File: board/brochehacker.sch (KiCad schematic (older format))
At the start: 5 parts, among them IC1 ATTINY85-P, P1 CONN_01X02, U1 MAX7219

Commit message: adição de chave de força
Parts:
- added SW1: SPST, Buttons_Switches_ThroughHole:SW_DIP_x1_Slide, symbol SPST
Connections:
- wire segments 53 -> 52
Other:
- moved on the sheet: P1
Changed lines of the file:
@@
 L CONN_01X02 P1
 U 1 1 579A841D
-P 7650 4800
-F 0 "P1" H 7650 4950 50  0000 C CNN
-F 1 "CONN_01X02" V 7750 4800 50  0000 C CNN
-F 2 "Pin_Headers:Pin_Header_Straight_1x02" H 7650 4800 50  0001 C CNN
-F 3 "" H 7650 4800 50  0000 C CNN
-	1    7650 4800
+P 8200 4750
+F 0 "P1" H 8200 4900 50  0000 C CNN
+F 1 "CONN_01X02" V 8300 4750 50  0000 C CNN
+F 2 "Pin_Headers:Pin_Header_Straight_1x02" H 8200 4750 50  0001 C CNN
+F 3 "" H 8200 4750 50  0000 C CNN
+	1    8200 4750
 	1    0    0    -1
 $EndComp
-Text GLabel 7250 4750 0    60   Input ~ 0
+Text GLabel 6700 4700 0    60   Input ~ 0
 VCC
-Text GLabel 7250 4850 0    60   Input ~ 0
+Text GLabel 7800 4800 0    60   Input ~ 0
 GND
 Wire Wire Line
-	7250 4750 7450 4750
+	7800 4700 8000 4700
 Wire Wire Line
-	7250 4850 7450 4850
+	7800 4800 8000 4800
+$Comp
+L SPST SW1
+U 1 1 579FD200
+P 7300 4700
+F 0 "SW1" H 7300 4800 50  0000 C CNN
+F 1 "SPST" H 7300 4600 50  0000 C CNN
+F 2 "Buttons_Switches_ThroughHole:SW_DIP_x1_Slide" H 7300 4700 50  0001 C CNN
+F 3 "" H 7300 4700 50  0000 C CNN
+	1    7300 4700
+	-1   0    0    -1
+$EndComp
 Wire Wire Line
-	7350 4850 7350 4950
-Connection ~ 7350 4850
-Wire Wire Line
-	7350 4750 7350 4650
-Connection ~ 7350 4750
-$Comp
-L VCC #PWR01
-U 1 1 579A854E
-P 7350 4650
-F 0 "#PWR01" H 7350 4500 50  0001 C CNN
-F 1 "VCC" H 7350 4800 50  0000 C CNN
-F 2 "" H 7350 4650 50  0000 C CNN
-F 3 "" H 7350 4650 50  0000 C CNN
-	1    7350 4650
-	1    0    0    -1
-$EndComp
-$Comp
-L GND #PWR02
-U 1 1 579A856C
-P 7350 4950
-F 0 "#PWR02" H 7350 4700 50  0001 C CNN
-F 1 "GND" H 7350 4800 50  0000 C CNN
-F 2 "" H 7350 4950 50  0000 C CNN
-F 3 "" H 7350 4950 50  0000 C CNN
-	1    7350 4950
-	1    0    0    -1
-$EndComp
+	6700 4700 6800 4700
 $EndSCHEMATC

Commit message: versão camada simples
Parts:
- removed IC1: ATTINY85-P, Housings_DIP:DIP-8_W7.62mm, symbol ATTINY85-P
- removed SW1: SPST, Buttons_Switches_ThroughHole:SW_DIP_x1_Slide, symbol SPST
- removed U1: MAX7219, Housings_DIP:DIP-24_W7.62mm, symbol MAX7219
- added C1, C3: 22pF, Capacitors_ThroughHole:C_Disc_D3_P2.5, symbol C
- added C2: 100uF, Capacitors_ThroughHole:C_Radial_D5_L6_P2.5, symbol CP
- added IC1: ATMEGA328-P, Housings_DIP:DIP-28_W7.62mm_LongPads, symbol ATMEGA328-P
- added Y1: 16MHz, Crystals:Crystal_HC50-U_Vertical, symbol Crystal
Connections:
- net GND: now also C2.2, IC1.22 (GND), IC1.8 (GND)
- net VCC: now also P1.1 (P1), C1.2, C2.1, C3.2, IC1.20 (AVCC), IC1.7 (VCC)
- net at R1.2: now also IC1.1 ((PCINT14/~RESET~)PC6)
- net DIG0 renamed ROW1
- net ROW1: now also IC1.15 ((PCINT1/OC1A)PB1)
- net DIG1 renamed ROW2
- net ROW2: now also IC1.26 ((PCINT11/ADC3)PC3)
- net DIG2 renamed ROW3
- net ROW3: now also IC1.14 ((PCINT0/CLKO/ICP1)PB0)
- net DIG3 renamed ROW4
- net ROW4: now also IC1.24 ((PCINT9/ADC1)PC1)
- net DIG4 renamed ROW5
- net ROW5: now also IC1.2 ((PCINT16/RXD)PD0)
- net DIG5 renamed ROW6
- net ROW6: now also IC1.13 ((PCINT23/AIN1)PD7)
- net DIG6 renamed ROW7
- net ROW7: now also IC1.3 ((PCINT17/TXD)PD1)
- net DIG7 renamed ROW8
- net ROW8: now also IC1.11 ((PCINT21/OC0B/T1)PD5)
- net SEGA renamed COL2
- net COL2: now also IC1.4 ((PCINT18/INT0)PD2)
- net SEGB renamed COL3
- net COL3: now also IC1.5 ((PCINT19/OC2B/INT1)PD3)
- net SEGC renamed COL4
- net COL4: now also IC1.16 ((PCINT2/OC1B/~SS~)PB2)
- net SEGD renamed COL5
- net COL5: now also IC1.12 ((PCINT22/OC0A/AIN0)PD6)
- net SEGDP renamed COL1
- net COL1: now also IC1.25 ((PCINT10/ADC2)PC2)
- net SEGE renamed COL6
- net COL6: now also IC1.23 ((PCINT8/ADC0)PC0)
- net SEGF renamed COL7
- net COL7: now also IC1.27 ((PCINT12/SDA/ADC4)PC4)
- net SEGG renamed COL8
- net COL8: now also IC1.28 ((PCINT13/SCL/ADC5)PC5)
- new net: C1.1, IC1.10 ((PCINT7/XTAL2/TOSC2)PB7), Y1.1
- new net: C3.1, IC1.9 ((PCINT6/XTAL1/TOSC1)PB6), Y1.2

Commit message: conserta cristal e reajusta jumpers
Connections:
- net GND: now also C1.2, C3.2
- net VCC: no longer C1.2, C3.2
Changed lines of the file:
@@
 	1    0    0    -1
 $EndComp
-Text GLabel 7600 2600 2    60   Input ~ 0
-VCC
 Text GLabel 3550 2000 0    60   Input ~ 0
 VCC
@@
 	3700 3050 3700 2000
 Connection ~ 3700 2000
+Text GLabel 7600 2600 2    60   Input ~ 0
+GND
 $EndSCHEMATC

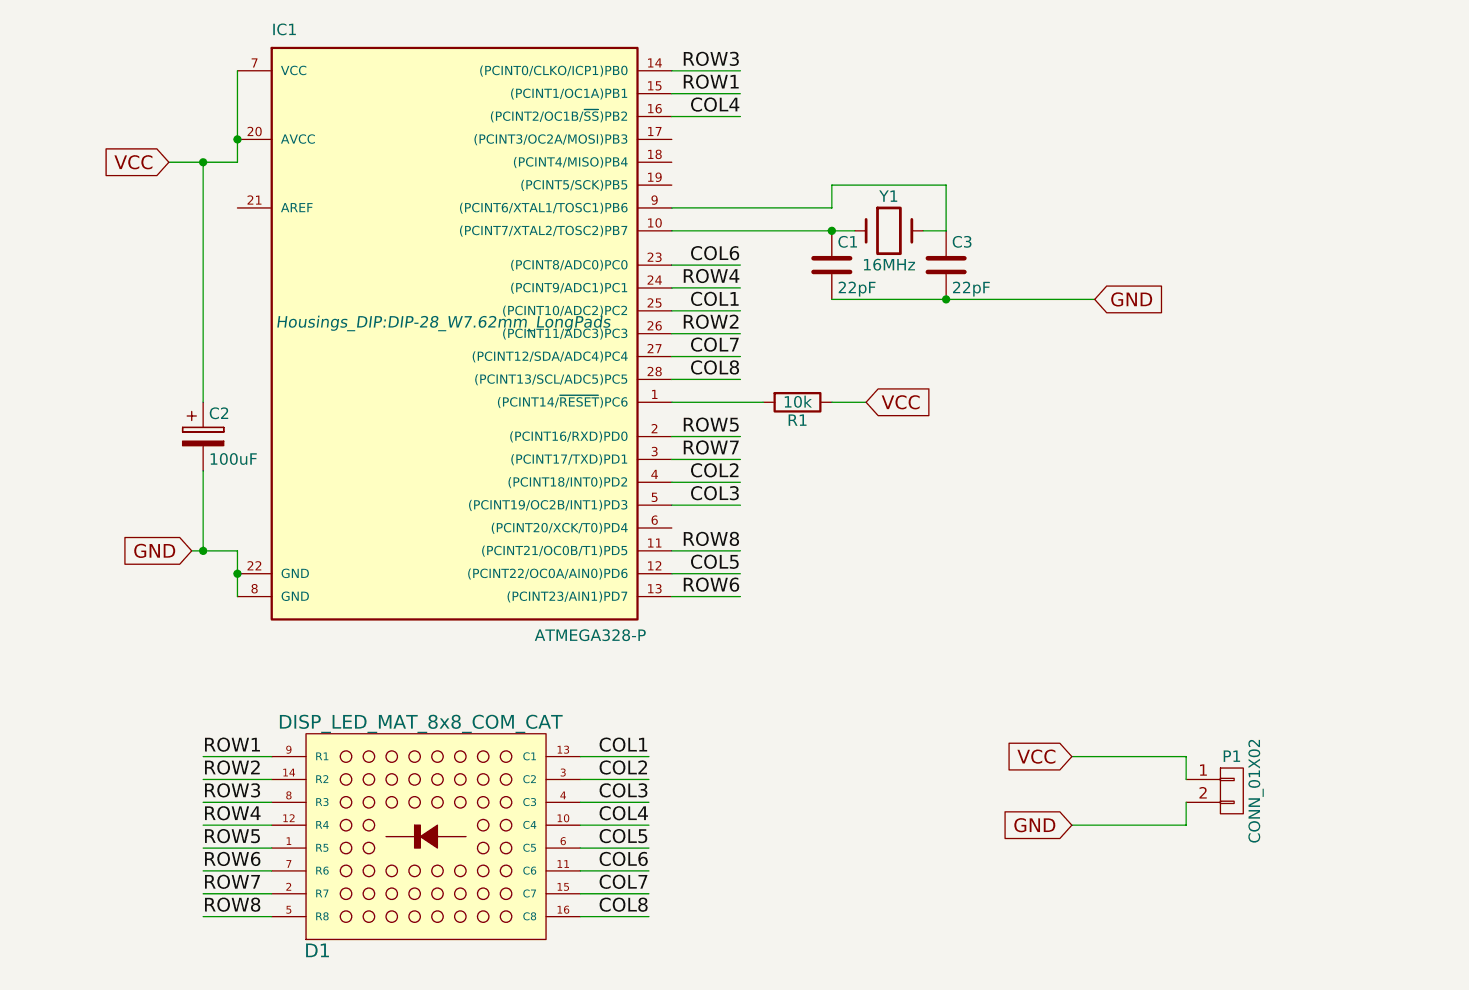
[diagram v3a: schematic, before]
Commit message: remove cristal, adiciona botões
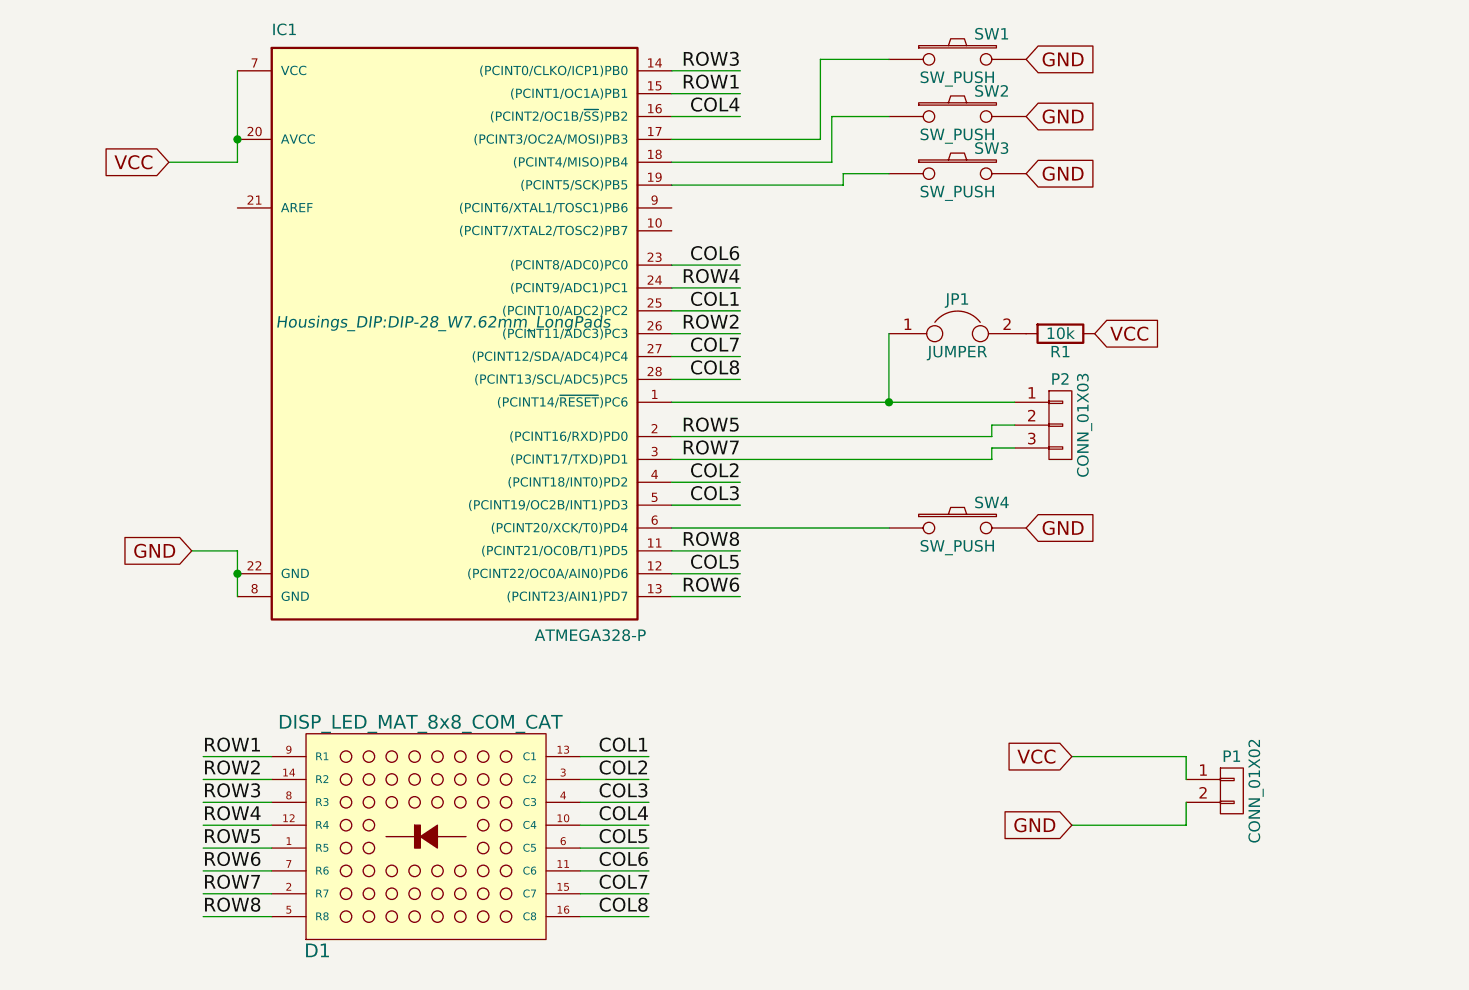
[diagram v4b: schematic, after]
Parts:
- removed C1, C3: 22pF, Capacitors_ThroughHole:C_Disc_D3_P2.5, symbol C
- removed C2: 100uF, Capacitors_ThroughHole:C_Radial_D5_L6_P2.5, symbol CP
- removed Y1: 16MHz, Crystals:Crystal_HC50-U_Vertical, symbol Crystal
- added JP1: JUMPER, Pin_Headers:Pin_Header_Straight_1x02, symbol JUMPER
- added P2: CONN_01X03, Pin_Headers:Pin_Header_Straight_1x03, symbol CONN_01X03
- added SW1, SW2, SW3, SW4: SW_PUSH, Buttons_Switches_ThroughHole:SW_PUSH_SMALL, symbol SW_PUSH
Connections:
- net GND: now also SW1.2, SW2.2, SW3.2, SW4.2
- net ROW5: now also P2.2 (P2)
- net ROW7: now also P2.3 (P3)
- net at IC1.1 ((PCINT14/~RESET~)PC6): now also JP1.1, P2.1 (P1); no longer R1.2
- net at IC1.17 ((PCINT3/OC2A/MOSI)PB3): now also SW1.1
- net at IC1.18 ((PCINT4/MISO)PB4): now also SW2.1
- net at IC1.19 ((PCINT5/SCK)PB5): now also SW3.1
- net at IC1.6 ((PCINT20/XCK/T0)PD4): now also SW4.1
- new net: JP1.2, R1.2
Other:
- moved on the sheet: R1
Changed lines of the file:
@@
 GND
-$Comp
-L CP C2
-U 1 1 57A24D52
-P 3700 3200
-F 0 "C2" H 3725 3300 50  0000 L CNN
-F 1 "100uF" H 3725 3100 50  0000 L CNN
-F 2 "Capacitors_ThroughHole:C_Radial_D5_L6_P2.5" H 3738 3050 50  0001 C CNN
-F 3 "" H 3700 3200 50  0000 C CNN
-	1    3700 3200
-	1    0    0    -1
-$EndComp
 $Comp
 L R R1
 U 1 1 57A24E82
-P 6300 3050
-F 0 "R1" V 6380 3050 50  0000 C CNN
-F 1 "10k" V 6300 3050 50  0000 C CNN
-F 2 "Resistors_ThroughHole:Resistor_Horizontal_RM7mm" V 6230 3050 50  0001 C CNN
-F 3 "" H 6300 3050 50  0000 C CNN
-	1    6300 3050
+P 7450 2750
+F 0 "R1" V 7530 2750 50  0000 C CNN
+F 1 "10k" V 7450 2750 50  0000 C CNN
+F 2 "Resistors_ThroughHole:Resistor_Horizontal_RM7mm" V 7380 2750 50  0001 C CNN
+F 3 "" H 7450 2750 50  0000 C CNN
+	1    7450 2750
 	0    1    1    0
 $EndComp
-Text GLabel 6600 3050 2    60   Input ~ 0
+Text GLabel 7600 2750 2    60   Input ~ 0
 VCC
-$Comp
-L Crystal Y1
-U 1 1 57A250DA
-P 6700 2300
-F 0 "Y1" H 6700 2450 50  0000 C CNN
-F 1 "16MHz" H 6700 2150 50  0000 C CNN
-F 2 "Crystals:Crystal_HC50-U_Vertical" H 6700 2300 50  0001 C CNN
-F 3 "" H 6700 2300 50  0000 C CNN
-	1    6700 2300
-	1    0    0    -1
-$EndComp
-$Comp
-L C C1
-U 1 1 57A25154
-P 6450 2450
-F 0 "C1" H 6475 2550 50  0000 L CNN
-F 1 "22pF" H 6475 2350 50  0000 L CNN
-F 2 "Capacitors_ThroughHole:C_Disc_D3_P2.5" H 6488 2300 50  0001 C CNN
-F 3 "" H 6450 2450 50  0000 C CNN
-	1    6450 2450
-	1    0    0    -1
-$EndComp
-$Comp
-L C C3
-U 1 1 57A251BC
-P 6950 2450
-F 0 "C3" H 6975 2550 50  0000 L CNN
-F 1 "22pF" H 6975 2350 50  0000 L CNN
-F 2 "Capacitors_ThroughHole:C_Disc_D3_P2.5" H 6988 2300 50  0001 C CNN
-F 3 "" H 6950 2450 50  0000 C CNN
-	1    6950 2450
-	1    0    0    -1
-$EndComp
 Text GLabel 3550 2000 0    60   Input ~ 0
 VCC
@@
 	6050 3700 5750 3700
 Wire Wire Line
-	6050 3300 5750 3300
+	5750 3300 7150 3300
 Wire Wire Line
 	6050 3900 5750 3900
 Wire Wire Line
-	6050 3200 5750 3200
+	5750 3200 7150 3200
 Wire Wire Line
 	6050 2550 5750 2550
@@
 	7500 4900 8000 4900
 Wire Wire Line
-	5750 3050 6150 3050
-Wire Wire Line
-	6600 3050 6450 3050
-Wire Wire Line
-	6950 2300 6850 2300
-Wire Wire Line
-	5750 2300 6550 2300
-Wire Wire Line
-	6450 2600 7600 2600
-Connection ~ 6450 2300
-Wire Wire Line
-	5750 2200 6450 2200
-Wire Wire Line
-	6450 2200 6450 2100
-Wire Wire Line
-	6450 2100 6950 2100
-Wire Wire Line
-	6950 2100 6950 2300
-Connection ~ 6950 2600
+	5750 3050 7250 3050
 Wire Wire Line
 	3850 1600 3850 2000
@@
 	3650 3700 3850 3700
 Connection ~ 3850 3800
-Wire Wire Line
-	3700 3350 3700 3700
-Connection ~ 3700 3700
-Wire Wire Line
-	3700 3050 3700 2000
-Connection ~ 3700 2000
-Text GLabel 7600 2600 2    60   Input ~ 0
-GND
+$Comp
+L SW_PUSH SW4
+U 1 1 57A927FF
+P 7000 3600
+F 0 "SW4" H 7150 3710 50  0000 C CNN
+F 1 "SW_PUSH" H 7000 3520 50  0000 C CNN
+F 2 "Buttons_Switches_ThroughHole:SW_PUSH_SMALL" H 7000 3600 50  0001 C CNN
+F 3 "" H 7000 3600 50  0000 C CNN
+	1    7000 3600
+	1    0    0    -1
+$EndComp
+$Comp
+L SW_PUSH SW3
+U 1 1 57A92846
+P 7000 2050
+F 0 "SW3" H 7150 2160 50  0000 C CNN
+F 1 "SW_PUSH" H 7000 1970 50  0000 C CNN
+F 2 "Buttons_Switches_ThroughHole:SW_PUSH_SMALL" H 7000 2050 50  0001 C CNN
+F 3 "" H 7000 2050 50  0000 C CNN
+	1    7000 2050
+	1    0    0    -1
+$EndComp
+$Comp
+L SW_PUSH SW2
+U 1 1 57A92895
+P 7000 1800
+F 0 "SW2" H 7150 1910 50  0000 C CNN
+F 1 "SW_PUSH" H 7000 1720 50  0000 C CNN
+F 2 "Buttons_Switches_ThroughHole:SW_PUSH_SMALL" H 7000 1800 50  0001 C CNN
+F 3 "" H 7000 1800 50  0000 C CNN
+	1    7000 1800
+	1    0    0    -1
+$EndComp
+$Comp
+L SW_PUSH SW1
+U 1 1 57A928C7
+P 7000 1550
+F 0 "SW1" H 7150 1660 50  0000 C CNN
+F 1 "SW_PUSH" H 7000 1470 50  0000 C CNN
+F 2 "Buttons_Switches_ThroughHole:SW_PUSH_SMALL" H 7000 1550 50  0001 C CNN
+F 3 "" H 7000 1550 50  0000 C CNN
+	1    7000 1550
+	1    0    0    -1
+$EndComp
+$Comp
+L CONN_01X03 P2
+U 1 1 57A92B5E
+P 7450 3150
+F 0 "P2" H 7450 3350 50  0000 C CNN
+F 1 "CONN_01X03" V 7550 3150 50  0000 C CNN
+F 2 "Pin_Headers:Pin_Header_Straight_1x03" H 7450 3150 50  0001 C CNN
+F 3 "" H 7450 3150 50  0000 C CNN
+	1    7450 3150
+	1    0    0    -1
+$EndComp
+$Comp
+L JUMPER JP1
+U 1 1 57A92DDA
+P 7000 2750
+F 0 "JP1" H 7000 2900 50  0000 C CNN
+F 1 "JUMPER" H 7000 2670 50  0000 C CNN
+F 2 "Pin_Headers:Pin_Header_Straight_1x02" H 7000 2750 50  0001 C CNN
+F 3 "" H 7000 2750 50  0000 C CNN
+	1    7000 2750
+	1    0    0    -1
+$EndComp
+Wire Wire Line
+	7150 3200 7150 3150
+Wire Wire Line
+	7150 3150 7250 3150
+Wire Wire Line
+	7150 3300 7150 3250
+Wire Wire Line
+	7150 3250 7250 3250
+Wire Wire Line
+	6700 2750 6700 3050
+Connection ~ 6700 3050
+Wire Wire Line
+	5750 1900 6400 1900
+Wire Wire Line
+	6400 1900 6400 1550
+Wire Wire Line
+	6400 1550 6700 1550
+Wire Wire Line
+	5750 2000 6450 2000
+Wire Wire Line
+	6450 2000 6450 1800
+Wire Wire Line
+	6450 1800 6700 1800
+Wire Wire Line
+	5750 2100 6500 2100
+Wire Wire Line
+	6500 2100 6500 2050
+Wire Wire Line
+	6500 2050 6700 2050
+Text GLabel 7300 1550 2    60   Input ~ 0
+GND
+Text GLabel 7300 1800 2    60   Input ~ 0
+GND
+Text GLabel 7300 2050 2    60   Input ~ 0
+GND
+Text GLabel 7300 3600 2    60   Input ~ 0
+GND
+Wire Wire Line
+	6700 3600 5750 3600
 $EndSCHEMATC

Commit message: remoção de jumper e traços mais grossos
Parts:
- removed JP1: JUMPER, Pin_Headers:Pin_Header_Straight_1x02, symbol JUMPER
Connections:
- net at IC1.1 ((PCINT14/~RESET~)PC6), P2.1 (P1): now also R1.2
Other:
- moved on the sheet: R1
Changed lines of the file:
@@
 L R R1
 U 1 1 57A24E82
-P 7450 2750
-F 0 "R1" V 7530 2750 50  0000 C CNN
-F 1 "10k" V 7450 2750 50  0000 C CNN
-F 2 "Resistors_ThroughHole:Resistor_Horizontal_RM7mm" V 7380 2750 50  0001 C CNN
-F 3 "" H 7450 2750 50  0000 C CNN
-	1    7450 2750
+P 6850 2750
+F 0 "R1" V 6930 2750 50  0000 C CNN
+F 1 "10k" V 6850 2750 50  0000 C CNN
+F 2 "Resistors_ThroughHole:Resistor_Horizontal_RM7mm" V 6780 2750 50  0001 C CNN
+F 3 "" H 6850 2750 50  0000 C CNN
+	1    6850 2750
 	0    1    1    0
 $EndComp
-Text GLabel 7600 2750 2    60   Input ~ 0
+Text GLabel 7000 2750 2    60   Input ~ 0
 VCC
 Text GLabel 3550 2000 0    60   Input ~ 0
@@
 	1    0    0    -1
 $EndComp
-$Comp
-L JUMPER JP1
-U 1 1 57A92DDA
-P 7000 2750
-F 0 "JP1" H 7000 2900 50  0000 C CNN
-F 1 "JUMPER" H 7000 2670 50  0000 C CNN
-F 2 "Pin_Headers:Pin_Header_Straight_1x02" H 7000 2750 50  0001 C CNN
-F 3 "" H 7000 2750 50  0000 C CNN
-	1    7000 2750
-	1    0    0    -1
-$EndComp
